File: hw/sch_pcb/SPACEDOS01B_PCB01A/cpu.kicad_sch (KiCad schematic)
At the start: 24 parts, among them J19 HEADER_2x01_PARALLEL, J22 HEADER_2x03, J4 HEADER_1x01, J5 HEADER_1x01, J6 HEADER_1x01, J7 HEADER_1x01, U10 ATMEGA1284P-AU, U11 PCF85263A, Y2 ABS07-120-32.768KHZ-T

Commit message: Update designs to KiCAD 6. Update schematics datasheet links Minor schematics improvements (titleblocks, schematics layout)
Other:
- company: (none) -> www.ust.cz
- title: (none) -> SPACEDOS01B
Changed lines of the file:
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@@
 (kicad_sch (version 20211123) (generator eeschema)
   (paper "A4")
+  (title_block
+    (title "SPACEDOS01B")
+    (date "2023-01-26")
+    (company "www.ust.cz")
+    (comment 1 "Semiconductor \\nIonizing radiation \\nsatellite spectrometer  \\nand dosimeter ")
+    (comment 3 "Universal Scientific Technologies s.r.o. ")
+  )
   (junction (at 19.05 20.32) (diameter 0) (color 0 0 0 0)
   )

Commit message: Correcly setup automation workflows and cleanup KiCAD project.
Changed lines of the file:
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@@
+    (stroke (width 0) (type default) (color 0 0 0 0))
+  )
+  (wire (pts (xy 63.5 18.415) (xy 63.5 20.32))
     (stroke (width 0) (type default) (color 0 0 0 0))
   )
@@
     (in_bom yes) (on_board yes)
     (property "Reference" "L1" (id 0) (at 53.34 15.494 90))
-    (property "Value" "10uH - LQH32CN100K23L" (id 1) (at 53.34 17.8054 90))
+    (property "Value" "10uH - LQH32CN100K23L" (id 1) (at 46.355 17.78 90))
     (property "Footprint" "Mlab_R:SMD-1210" (id 2) (at 53.34 20.32 0)
       (effects (font (size 1.27 1.27)) hide)
@@
       (effects (font (size 1.27 1.27)) hide)
     )
+    (pin "1")
+  )
+  (symbol (lib_id "power:PWR_FLAG") (at 63.5 18.415 0) (unit 1)
+    (in_bom yes) (on_board yes) (fields_autoplaced)
+    (property "Reference" "#FLG0109" (id 0) (at 63.5 16.51 0)
+      (effects (font (size 1.27 1.27)) hide)
+    )
+    (property "Value" "PWR_FLAG" (id 1) (at 63.5 14.8392 0))
+    (property "Footprint" "" (id 2) (at 63.5 18.415 0)
+      (effects (font (size 1.27 1.27)) hide)
+    )
+    (property "Datasheet" "~" (id 3) (at 63.5 18.415 0)
+      (effects (font (size 1.27 1.27)) hide)
+    )

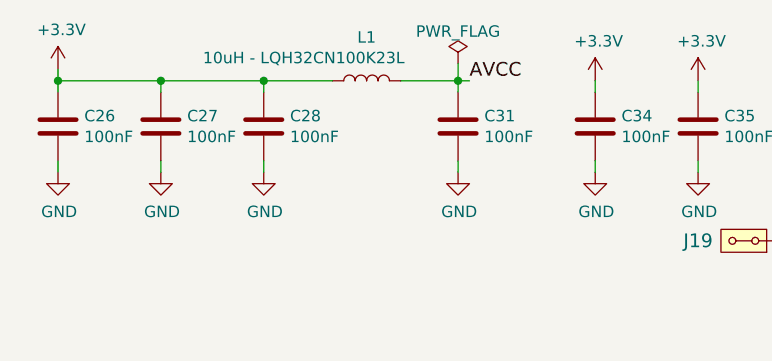
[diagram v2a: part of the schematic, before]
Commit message: Center PCB in page. Improve dimensions.
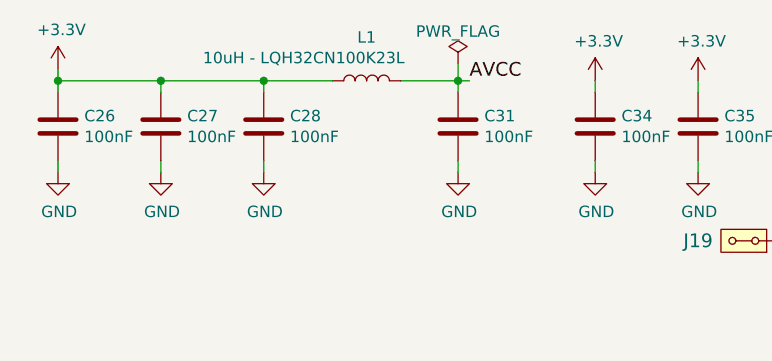
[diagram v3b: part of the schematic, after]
